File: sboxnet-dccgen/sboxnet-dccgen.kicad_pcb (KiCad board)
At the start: 2 copper layers, 28 x 47 mm, 15 parts, among them J1 sboxnet-stecker_02x17, J2 Screw_Terminal_01x02, U1 SN65HVD230

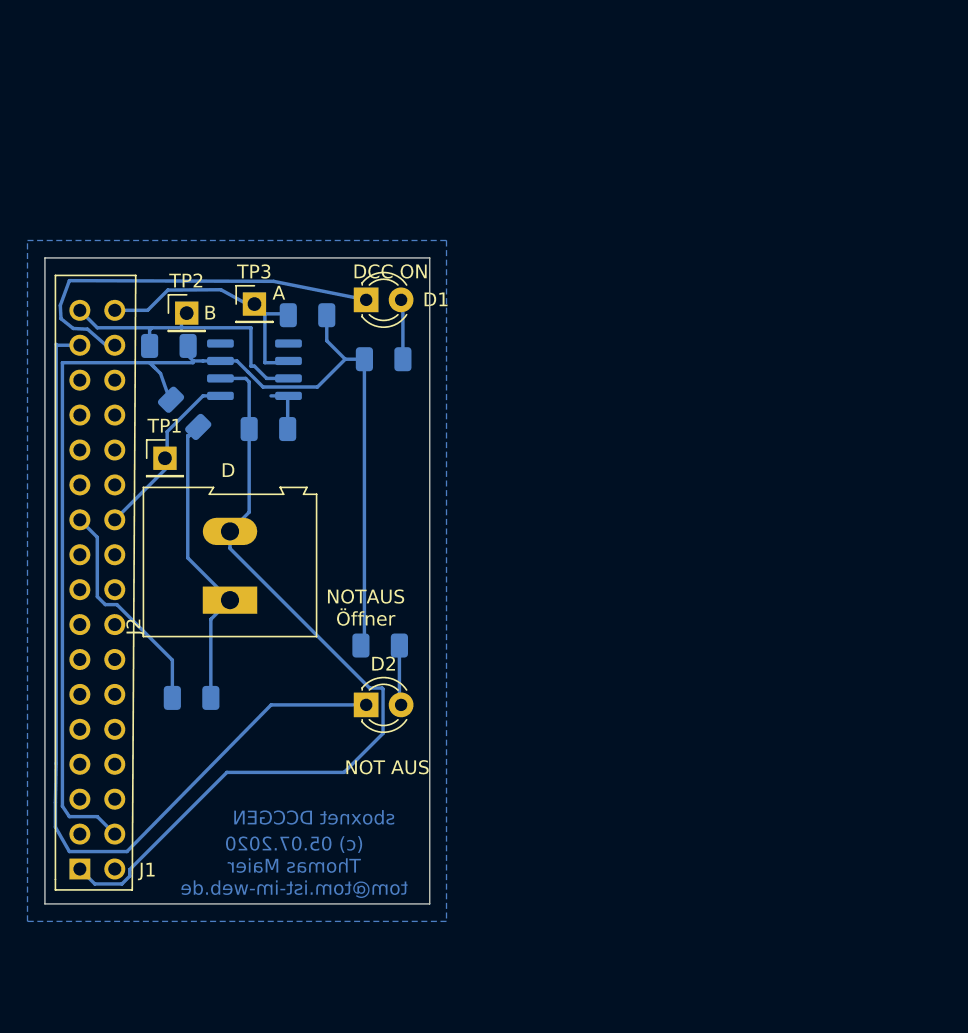
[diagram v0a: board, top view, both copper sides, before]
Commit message: neuer DCCGEN mit sboxnet Verteiler und Abschlusswiderstanden
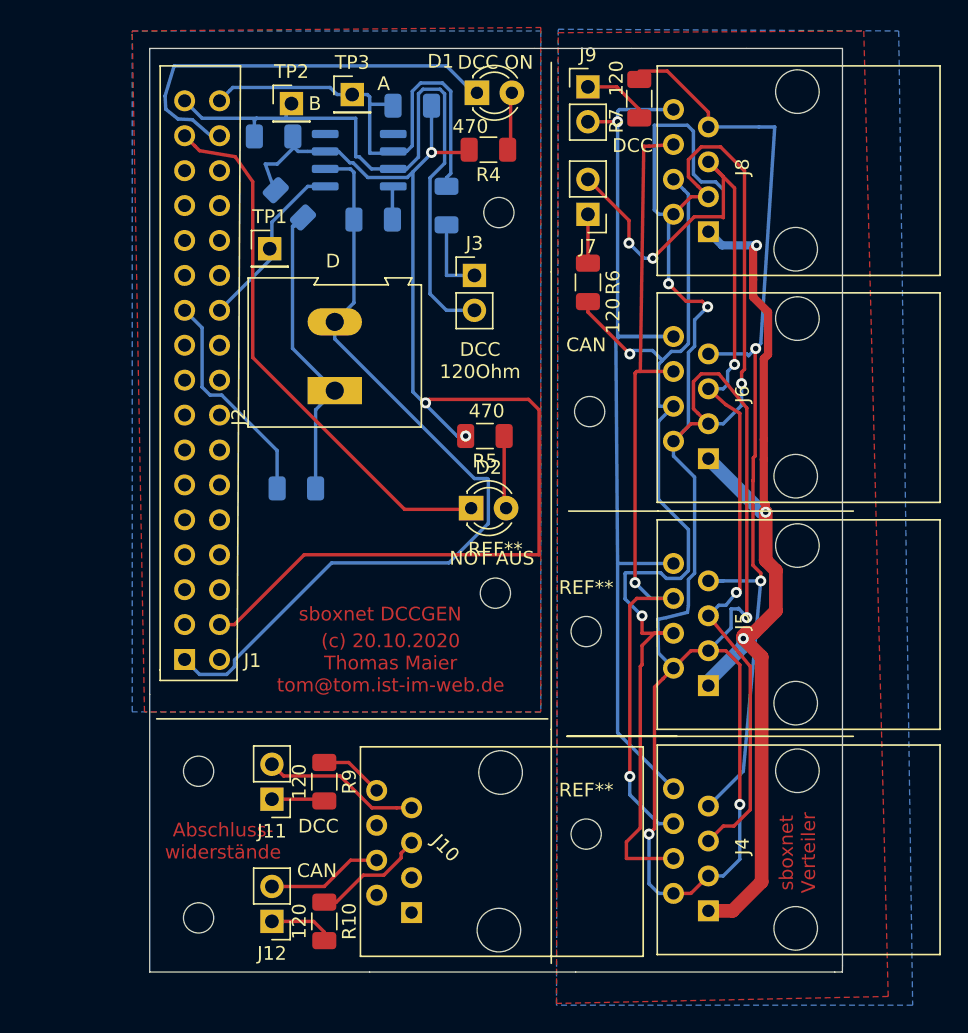
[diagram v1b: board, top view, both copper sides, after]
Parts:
- added J10: 8P8C, sboxnet:8p8c-mebp, F.Cu at (59.7, 92.7)
- added J11: Conn_01x02, Connector_PinHeader_2.54mm:PinHeader_1x02_P2.54mm_Vertical, F.Cu at (43.2, 88.9)
- added J12: Conn_01x02, Connector_PinHeader_2.54mm:PinHeader_1x02_P2.54mm_Vertical, F.Cu at (43.2, 97.8)
- added J3: Conn_01x02, Connector_PinHeader_2.54mm:PinHeader_1x02_P2.54mm_Vertical, F.Cu at (57.9, 50.8)
- added J4: 8P8C, sboxnet:8p8c-mebp, F.Cu at (81.3, 92.6)
- added J5: 8P8C, sboxnet:8p8c-mebp, F.Cu at (81.3, 76.2)
- added J6: 8P8C, sboxnet:8p8c-mebp, F.Cu at (81.3, 59.7)
- added J7: Conn_01x02, Connector_PinHeader_2.54mm:PinHeader_1x02_P2.54mm_Vertical, F.Cu at (66.2, 46.4)
- added J8: 8P8C, sboxnet:8p8c-mebp, F.Cu at (81.3, 43.2)
- added J9: Conn_01x02, Connector_PinHeader_2.54mm:PinHeader_1x02_P2.54mm_Vertical, F.Cu at (66.2, 37.1)
- added R10: 120, Resistor_SMD:R_1206_3216Metric, F.Cu at (47.0, 97.8)
- added R6: 120, Resistor_SMD:R_1206_3216Metric, F.Cu at (66.2, 51.3)
- added R7  120: 120, Resistor_SMD:R_1206_3216Metric, F.Cu at (69.9, 37.9)
- added R8: 120, Resistor_SMD:R_1206_3216Metric, B.Cu at (55.9, 45.7)
- added R9: 120, Resistor_SMD:R_1206_3216Metric, F.Cu at (47.0, 87.6)
- added REF**: MountingHole_2.2mm_M2, MountingHole:MountingHole_2.2mm_M2, F.Cu at (37.8, 97.5)
- added REF**: MountingHole_2.2mm_M2, MountingHole:MountingHole_2.2mm_M2, F.Cu at (37.8, 86.9)
- added REF**: MountingHole_2.2mm_M2, MountingHole:MountingHole_2.2mm_M2, F.Cu at (66.0, 91.4)
- added REF**: MountingHole_2.2mm_M2, MountingHole:MountingHole_2.2mm_M2, F.Cu at (66.0, 76.7)
- added REF**: MountingHole_2.2mm_M2, MountingHole:MountingHole_2.2mm_M2, F.Cu at (66.3, 60.7)
- added REF**: MountingHole_2.2mm_M2, MountingHole:MountingHole_2.2mm_M2, F.Cu at (59.4, 73.9)
- added REF**: MountingHole_2.2mm_M2, MountingHole:MountingHole_2.2mm_M2, F.Cu at (59.7, 46.2)
- D1: value LED -> gn
- D2: value LED -> rt
- R3: value 2,2k -> 1k
- R4, R5: value 680 -> 470; moved to F.Cu
- moved D1 17.1 mm to (58.1, 37.5)
- moved R2 17.0 mm to (45.0, 66.3)
- moved TP2 17.0 mm to (44.6, 38.3)
- moved U1 17.0 mm to (49.5, 42.4)
- moved R1 17.0 mm to (50.5, 46.7)
- moved R3 17.0 mm to (44.5, 45.6)
- moved R4 17.0 mm to (58.9, 41.7)
- moved R5 17.0 mm to (58.7, 62.5)
- moved R6 17.0 mm to (53.4, 38.5)
- moved J1 17.0 mm to (39.4, 81.3)
- moved J2 17.0 mm to (47.8, 59.2)
- moved R7 17.0 mm to (43.3, 40.7)
- moved TP1 17.0 mm to (43.0, 48.9)
- moved TP3 16.8 mm to (49.0, 37.6)
- moved D2 16.2 mm to (57.7, 67.7)
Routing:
- net +7_x: track 0.00 -> 163.9 mm, vias 0 -> 6
- net gnd_x: track 0.00 -> 129.3 mm, vias 0 -> 5
- net can_h_x: track 0.00 -> 76.0 mm, vias 0 -> 4
- net can_l_x: track 0.00 -> 74.9 mm, vias 0 -> 2
- net dcc_a_x: track 0.00 -> 71.7 mm, vias 0 -> 2
- net dcc_b_x: track 0.00 -> 69.4 mm, vias 0 -> 1
- net DCC_B: track 21.4 -> 49.1 mm
- net PD7: track 65.0 -> 39.3 mm
- net DCC_A: track 19.0 -> 35.1 mm
- net Net-(J10-Pad7): track 0.00 -> 11.5 mm
- net Net-(J10-Pad4): track 0.00 -> 8.41 mm
- net Net-(J10-Pad5): track 0.00 -> 8.34 mm
- net Net-(J3-Pad1): track 0.00 -> 5.71 mm
- net Net-(J9-Pad1): track 0.00 -> 5.04 mm
- net Net-(J12-Pad1): track 0.00 -> 4.76 mm
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- added copper zone on F.Cu, net +7_x
- added copper zone on F.Cu, net GND
- added copper zone on B.Cu, net gnd_x
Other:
- board size 28 x 47 mm -> 50.4 x 67.2 mm
- board text added: "(c) 20.10.2020 Thomas Maier tom@tom.ist-im-web.de"
- board text added: "Abschluss- widerstände"
- board text added: "CAN"
- board text added: "DCC"
- board text added: "DCC 120Ohm"
- board text added: "sboxnet Verteiler"
- board text removed: "(c) 05.07.2020 Thomas Maier tom@tom.ist-im-web.de"
- board text removed: "NOTAUS Öffner"

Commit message: dccgen bestellt
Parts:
- U1: value SN65HVD230 -> SN65...230
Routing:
- net gnd_x: track 129.3 -> 148.9 mm, vias 5 -> 10
- net dcc_b_x: track 69.4 -> 70.6 mm
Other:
- board text added: "DCC 120"
- board text removed: "DCC 120Ohm"

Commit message: fix dccgen layout
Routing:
- net +7_x: track 163.9 -> 153.5 mm
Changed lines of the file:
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@@
     (thickness 1.6)
     (drawings 34)
-    (tracks 449)
+    (tracks 446)
     (zones 0)
     (modules 37)
@@
   (segment (start 71.302999 78.282999) (end 71.247 75.819) (width 0.25) (layer B.Cu) (net 59))
   (segment (start 72.39 79.37) (end 71.302999 78.282999) (width 0.25) (layer B.Cu) (net 59))
-  (segment (start 71.31237 46.35) (end 70.993 46.03063) (width 0.25) (layer B.Cu) (net 59))
-  (segment (start 72.39 46.35) (end 71.31237 46.35) (width 0.25) (layer B.Cu) (net 59))
-  (segment (start 70.993 46.03063) (end 70.993 39.878) (width 0.25) (layer B.Cu) (net 59))
-  (segment (start 70.993 39.878) (end 73.406 39.878) (width 0.25) (layer B.Cu) (net 59))
   (segment (start 73.151999 62.098001) (end 72.39 62.86) (width 0.25) (layer B.Cu) (net 59))
   (segment (start 73.477001 56.403171) (end 73.477001 61.772999) (width 0.25) (layer B.Cu) (net 59))
-  (segment (start 75.451761 43.992999) (end 76.017001 44.558239) (width 0.25) (layer B.Cu) (net 59))
   (segment (start 73.477001 61.772999) (end 73.151999 62.098001) (width 0.25) (layer B.Cu) (net 59))
-  (segment (start 74.408239 43.992999) (end 75.451761 43.992999) (width 0.25) (layer B.Cu) (net 59))
-  (segment (start 73.842999 43.427759) (end 74.408239 43.992999) (width 0.25) (layer B.Cu) (net 59))
-  (segment (start 73.842999 40.314999) (end 73.842999 43.427759) (width 0.25) (layer B.Cu) (net 59))
-  (segment (start 73.406 39.878) (end 73.842999 40.314999) (width 0.25) (layer B.Cu) (net 59))
   (segment (start 76.00763 94.483) (end 77.216 93.27463) (width 0.25) (layer B.Cu) (net 59))
   (segment (start 74.93 94.483) (end 76.00763 94.483) (width 0.25) (layer B.Cu) (net 59))
@@
   (segment (start 73.66 61.59) (end 74.93 61.59) (width 0.25) (layer F.Cu) (net 59))
   (segment (start 72.39 62.86) (end 73.66 61.59) (width 0.25) (layer F.Cu) (net 59))
-  (segment (start 73.66 45.08) (end 74.93 45.08) (width 0.25) (layer F.Cu) (net 59))
-  (segment (start 72.39 46.35) (end 73.66 45.08) (width 0.25) (layer F.Cu) (net 59))
   (segment (start 73.92701 55.953162) (end 73.92701 54.03819) (width 0.25) (layer B.Cu) (net 59))
   (segment (start 73.477001 56.403171) (end 73.92701 55.953162) (width 0.25) (layer B.Cu) (net 59))
@@
   (segment (start 72.0344 46.7056) (end 72.39 46.35) (width 0.25) (layer B.Cu) (net 59))
   (segment (start 72.0344 51.4096) (end 72.0344 46.7056) (width 0.25) (layer B.Cu) (net 59))
+  (segment (start 74.168001 44.318001) (end 74.93 45.08) (width 0.25) (layer B.Cu) (net 59))
+  (segment (start 74.168001 43.979239) (end 74.168001 44.318001) (width 0.25) (layer B.Cu) (net 59))
+  (segment (start 72.911761 42.722999) (end 74.168001 43.979239) (width 0.25) (layer B.Cu) (net 59))
+  (segment (start 71.868239 42.722999) (end 72.911761 42.722999) (width 0.25) (layer B.Cu) (net 59))
+  (segment (start 71.302999 43.288239) (end 71.868239 42.722999) (width 0.25) (layer B.Cu) (net 59))
+  (segment (start 71.302999 46.340629) (end 71.302999 43.288239) (width 0.25) (layer B.Cu) (net 59))
+  (segment (start 71.31237 46.35) (end 71.302999 46.340629) (width 0.25) (layer B.Cu) (net 59))
+  (segment (start 72.39 46.35) (end 71.31237 46.35) (width 0.25) (layer B.Cu) (net 59))
   (zone (net 35) (net_name GND) (layer B.Cu) (hatch edge 0.508)
     (connect_pads (clearance 0.508))

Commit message: erneut dccgen
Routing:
- net dcc_b_x: track 70.6 -> 69.8 mm
- net gnd_x: track 148.9 -> 149.6 mm
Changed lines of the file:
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@@
     (thickness 1.6)
     (drawings 34)
-    (tracks 446)
+    (tracks 455)
     (zones 0)
     (modules 37)
@@
   (segment (start 78.3717 56.1213) (end 77.851 56.642) (width 0.25) (layer B.Cu) (net 44))
   (via (at 78.3717 56.1213) (size 0.8) (drill 0.4) (layers F.Cu B.Cu) (net 44))
-  (segment (start 72.39 71.755) (end 68.326 71.755) (width 0.25) (layer B.Cu) (net 45))
   (segment (start 68.453 38.735) (end 72.39 38.735) (width 0.25) (layer B.Cu) (net 45))
   (segment (start 68.326 38.862) (end 68.453 38.735) (width 0.25) (layer B.Cu) (net 45))
@@
   (via (at 68.326 39.624) (size 0.8) (drill 0.4) (layers F.Cu B.Cu) (net 45))
   (segment (start 68.326 39.624) (end 66.167 39.624) (width 0.25) (layer F.Cu) (net 45))
-  (segment (start 67.62496 85.43036) (end 72.39 88.138) (width 0.25) (layer B.Cu) (net 45))
-  (segment (start 68.326 71.755) (end 67.62496 85.43036) (width 0.25) (layer B.Cu) (net 45))
-  (segment (start 68.453 55.245) (end 72.39 55.245) (width 0.25) (layer B.Cu) (net 45))
-  (segment (start 68.199 55.499) (end 68.453 55.245) (width 0.25) (layer B.Cu) (net 45))
-  (segment (start 68.31076 71.81088) (end 68.199 55.499) (width 0.25) (layer B.Cu) (net 45))
+  (segment (start 72.39 71.755) (end 68.326 71.6788) (width 0.25) (layer B.Cu) (net 45))
+  (segment (start 69.4944 85.2424) (end 72.39 88.138) (width 0.25) (layer B.Cu) (net 45))
+  (segment (start 69.088 75.8444) (end 69.088 79.9084) (width 0.25) (layer B.Cu) (net 45))
+  (segment (start 67.5132 81.4832) (end 67.5132 85.2424) (width 0.25) (layer B.Cu) (net 45))
+  (segment (start 69.088 79.9084) (end 67.5132 81.4832) (width 0.25) (layer B.Cu) (net 45))
+  (segment (start 68.326 75.0824) (end 69.088 75.8444) (width 0.25) (layer B.Cu) (net 45))
+  (segment (start 67.5132 85.2424) (end 69.4944 85.2424) (width 0.25) (layer B.Cu) (net 45))
+  (segment (start 68.326 71.6788) (end 68.326 75.0824) (width 0.25) (layer B.Cu) (net 45))
+  (segment (start 67.6656 64.8208) (end 67.6656 71.0184) (width 0.25) (layer B.Cu) (net 45))
+  (segment (start 69.596 63.3476) (end 69.1388 63.3476) (width 0.25) (layer B.Cu) (net 45))
+  (segment (start 69.596 58.1152) (end 69.596 63.3476) (width 0.25) (layer B.Cu) (net 45))
+  (segment (start 68.256319 56.775519) (end 69.596 58.1152) (width 0.25) (layer B.Cu) (net 45))
+  (segment (start 68.256319 55.887599) (end 68.256319 56.775519) (width 0.25) (layer B.Cu) (net 45))
+  (segment (start 67.6656 71.0184) (end 68.326 71.6788) (width 0.25) (layer B.Cu) (net 45))
+  (segment (start 68.326 55.817918) (end 68.256319 55.887599) (width 0.25) (layer B.Cu) (net 45))
+  (segment (start 69.1388 63.3476) (end 67.6656 64.8208) (width 0.25) (layer B.Cu) (net 45))
+  (segment (start 68.326 55.245) (end 68.326 55.817918) (width 0.25) (layer B.Cu) (net 45))
   (segment (start 66.167 49.908) (end 66.167 46.355) (width 0.25) (layer F.Cu) (net 46))
   (segment (start 68.2622 37.084) (end 69.9008 38.7226) (width 0.25) (layer F.Cu) (net 47))
@@
   (segment (start 70.42404 66.93408) (end 70.42404 66.93408) (width 0.25) (layer F.Cu) (net 58))
   (via (at 70.42404 66.93408) (size 0.8) (drill 0.4) (layers F.Cu B.Cu) (net 58))
-  (segment (start 69.858355 66.93408) (end 69.838035 66.9544) (width 0.25) (layer B.Cu) (net 58))
-  (segment (start 70.42404 66.93408) (end 69.858355 66.93408) (width 0.25) (layer B.Cu) (net 58))
-  (segment (start 69.838035 66.9544) (end 69.07276 66.9544) (width 0.25) (layer B.Cu) (net 58))
   (segment (start 69.04736 66.9544) (end 69.04736 66.9544) (width 0.25) (layer B.Cu) (net 58))
-  (segment (start 69.07276 66.9544) (end 69.04736 66.9544) (width 0.25) (layer B.Cu) (net 58))
-  (via (at 69.07276 66.9544) (size 0.8) (drill 0.4) (layers F.Cu B.Cu) (net 58))
   (segment (start 67.39636 66.94424) (end 67.39636 66.94424) (width 0.25) (layer F.Cu) (net 58))
-  (segment (start 68.507075 66.9544) (end 69.07276 66.9544) (width 0.25) (layer F.Cu) (net 58))
-  (segment (start 68.496915 66.94424) (end 68.507075 66.9544) (width 0.25) (layer F.Cu) (net 58))
-  (segment (start 66.83756 66.91376) (end 68.496915 66.94424) (width 0.25) (layer F.Cu) (net 58))
-  (via (at 66.83756 66.91376) (size 0.8) (drill 0.4) (layers F.Cu B.Cu) (net 58))
-  (segment (start 73.918 80.64) (end 72.24676 82.31124) (width 0.25) (layer B.Cu) (net 58))
-  (segment (start 74.93 80.64) (end 73.918 80.64) (width 0.25) (layer B.Cu) (net 58))
-  (segment (start 72.24676 82.31124) (end 69.82968 82.31124) (width 0.25) (layer B.Cu) (net 58))
-  (segment (start 69.82968 82.31124) (end 69.04228 82.31124) (width 0.25) (layer B.Cu) (net 58))
-  (segment (start 69.04228 82.31124) (end 68.61048 82.31124) (width 0.25) (layer B.Cu) (net 58))
-  (segment (start 68.61048 82.31124) (end 68.31584 82.31124) (width 0.25) (layer B.Cu) (net 58))
-  (via (at 68.61048 82.31124) (size 0.8) (drill 0.4) (layers F.Cu B.Cu) (net 58))
-  (segment (start 68.61048 82.31124) (end 68.044795 82.31124) (width 0.25) (layer F.Cu) (net 58))
-  (segment (start 68.044795 82.31124) (end 66.17716 82.31124) (width 0.25) (layer F.Cu) (net 58))
   (segment (start 66.17716 82.31124) (end 66.17716 82.31124) (width 0.25) (layer F.Cu) (net 58))
   (via (at 66.17716 82.31124) (size 0.8) (drill 0.4) (layers F.Cu B.Cu) (net 58))
+  (segment (start 68.6816 66.9544) (end 69.04736 66.9544) (width 0.25) (layer B.Cu) (net 58))
+  (segment (start 69.858355 66.93408) (end 70.42404 66.93408) (width 0.25) (layer B.Cu) (net 58))
+  (segment (start 69.838035 66.9544) (end 69.858355 66.93408) (width 0.25) (layer B.Cu) (net 58))
+  (segment (start 68.6816 66.9544) (end 69.838035 66.9544) (width 0.25) (layer B.Cu) (net 58))
+  (via (at 68.6816 66.9544) (size 0.8) (drill 0.4) (layers F.Cu B.Cu) (net 58))
+  (segment (start 68.496915 66.94424) (end 68.507075 66.9544) (width 0.25) (layer F.Cu) (net 58))
+  (segment (start 66.3448 66.9544) (end 68.496915 66.94424) (width 0.25) (layer F.Cu) (net 58))
+  (segment (start 68.507075 66.9544) (end 68.6816 66.9544) (width 0.25) (layer F.Cu) (net 58))
+  (via (at 66.3448 66.9544) (size 0.8) (drill 0.4) (layers F.Cu B.Cu) (net 58))
+  (segment (start 68.044795 82.31124) (end 66.17716 82.31124) (width 0.25) (layer F.Cu) (net 58))
+  (segment (start 68.4784 82.31124) (end 68.044795 82.31124) (width 0.25) (layer F.Cu) (net 58))
+  (segment (start 73.918 80.64) (end 74.93 80.64) (width 0.25) (layer B.Cu) (net 58))
+  (segment (start 68.4784 82.31124) (end 72.24676 82.31124) (width 0.25) (layer B.Cu) (net 58))
+  (segment (start 68.4784 82.31124) (end 68.31584 82.31124) (width 0.25) (layer B.Cu) (net 58))
+  (segment (start 72.24676 82.31124) (end 73.918 80.64) (width 0.25) (layer B.Cu) (net 58))
+  (via (at 68.4784 82.31124) (size 0.8) (drill 0.4) (layers F.Cu B.Cu) (net 58))
   (segment (start 71.31237 95.753) (end 70.612 95.05263) (width 0.25) (layer B.Cu) (net 59))
   (segment (start 72.39 95.753) (end 71.31237 95.753) (width 0.25) (layer B.Cu) (net 59))

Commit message: dccgen Modul
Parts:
- added JP1: SolderJumper_3_Open, Jumper:SolderJumper-3_P1.3mm_Open_Pad1.0x1.5mm, F.Cu at (46.0, 69.2)
- added JP2: SolderJumper_3_Open, Jumper:SolderJumper-3_P1.3mm_Open_Pad1.0x1.5mm, F.Cu at (46.0, 71.9)
- added JP3: SolderJumper_3_Open, Jumper:SolderJumper-3_P1.3mm_Open_Pad1.0x1.5mm, F.Cu at (46.0, 74.5)
- R7: renamed from R7  120
- U1: value SN65...230 -> SN65HVD230
- moved D1 0.10 mm to (58.0, 37.5)
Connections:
- J1 pad 1: Net-(J1-Pad1) -> unconnected-(J1-Pad1)
- J1 pad 10: Net-(J1-Pad10) -> unconnected-(J1-Pad10)
- J1 pad 11: Net-(J1-Pad11) -> unconnected-(J1-Pad11)
- J1 pad 12: Net-(J1-Pad12) -> unconnected-(J1-Pad12)
- J1 pad 13: Net-(J1-Pad13) -> PB0
- J1 pad 14: Net-(J1-Pad14) -> PB1
- J1 pad 15: Net-(J1-Pad15) -> PB2
- J1 pad 16: Net-(J1-Pad16) -> unconnected-(J1-Pad16)
- J1 pad 17: Net-(J1-Pad17) -> unconnected-(J1-Pad17)
- J1 pad 18: Net-(J1-Pad18) -> unconnected-(J1-Pad18)
- J1 pad 19: Net-(J1-Pad19) -> unconnected-(J1-Pad19)
- J1 pad 20: Net-(J1-Pad20) -> unconnected-(J1-Pad20)
- J1 pad 23: Net-(J1-Pad23) -> unconnected-(J1-Pad23)
- J1 pad 24: Net-(J1-Pad24) -> unconnected-(J1-Pad24)
- J1 pad 25: Net-(J1-Pad25) -> unconnected-(J1-Pad25)
- J1 pad 26: Net-(J1-Pad26) -> unconnected-(J1-Pad26)
- J1 pad 27: Net-(J1-Pad27) -> unconnected-(J1-Pad27)
- J1 pad 28: Net-(J1-Pad28) -> unconnected-(J1-Pad28)
- J1 pad 29: Net-(J1-Pad29) -> unconnected-(J1-Pad29)
- J1 pad 30: Net-(J1-Pad30) -> unconnected-(J1-Pad30)
- J1 pad 4: Net-(J1-Pad4) -> unconnected-(J1-Pad4)
- J1 pad 5: Net-(J1-Pad5) -> unconnected-(J1-Pad5)
- J1 pad 6: Net-(J1-Pad6) -> unconnected-(J1-Pad6)
- J1 pad 7: Net-(J1-Pad7) -> unconnected-(J1-Pad7)
- J1 pad 8: Net-(J1-Pad8) -> unconnected-(J1-Pad8)
- J1 pad 9: Net-(J1-Pad9) -> unconnected-(J1-Pad9)
- J10 pad 1: Net-(J10-Pad1) -> unconnected-(J10-Pad1)
- J10 pad 2: Net-(J10-Pad2) -> unconnected-(J10-Pad2)
- J10 pad 3: Net-(J10-Pad3) -> unconnected-(J10-Pad3)
- J10 pad 6: Net-(J10-Pad6) -> unconnected-(J10-Pad6)
- U1 pad 4: Net-(U1-Pad4) -> unconnected-(U1-Pad4)
- U1 pad 5: Net-(U1-Pad5) -> unconnected-(U1-Pad5)
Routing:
- net GND: track 61.0 -> 11.2 mm, vias 0 -> 1
- net PB1: track 0.00 -> 16.9 mm
- net PB0: track 0.00 -> 15.3 mm
- net PB2: track 0.00 -> 11.0 mm
- net +3V3: track 90.3 -> 84.9 mm, vias 3 -> 5
- net PD7: track 39.3 -> 41.2 mm
- removed copper zone on B.Cu, net GND
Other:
- net class Default removed

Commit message: gbm
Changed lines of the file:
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@@
   (segment (start 77.47 77.0128) (end 77.690799 76.792001) (width 1) (layer "F.Cu") (net 56))
   (segment (start 68.4784 82.31124) (end 68.044795 82.31124) (width 0.25) (layer "F.Cu") (net 56))
-  (segment (start 79.0956 71.522942) (end 79.0956 68.0212) (width 1) (layer "F.Cu") (net 56))
+  (segment (start 79.0956 71.522942) (end 79.0956 68.0212) (width 0.8) (layer "F.Cu") (net 56))
   (segment (start 79.0956 68.0212) (end 79.0956 67.455515) (width 0.6) (layer "F.Cu") (net 56))
   (segment (start 78.95861 64.195683) (end 78.95861 62.738) (width 0.6) (layer "F.Cu") (net 56))
@@
   (segment (start 79.271701 53.465301) (end 78.185011 52.378611) (width 0.6) (layer "F.Cu") (net 56))
   (segment (start 69.723 57.785) (end 72.39 57.785) (width 0.25) (layer "F.Cu") (net 56))
-  (segment (start 79.271701 56.553301) (end 79.271701 53.465301) (width 0.6) (layer "F.Cu") (net 56))
+  (segment (start 79.271701 56.553301) (end 79.271701 53.465301) (width 0.4) (layer "F.Cu") (net 56))
   (segment (start 78.185011 48.865789) (end 78.4352 48.6156) (width 0.6) (layer "F.Cu") (net 56))
   (segment (start 69.596 57.912) (end 69.723 57.785) (width 0.25) (layer "F.Cu") (net 56))
